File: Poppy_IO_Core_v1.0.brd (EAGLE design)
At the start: 67.6 x 31.8 mm, 97 parts, among them IC3 ATMEGA2560-16AU, IC6 LP2985-33DBVR, Q1 16MHz, Q2 16MHz, Q3 16MHz, Q4 16MHz, Q5 24MHz, U1 ATmega16u2, U2 MPU-6000, U3 USB2514B-AEZC, U4 ATmega16u2, U5 ATmega16u2, X1 1376408-SLOT_1.8V

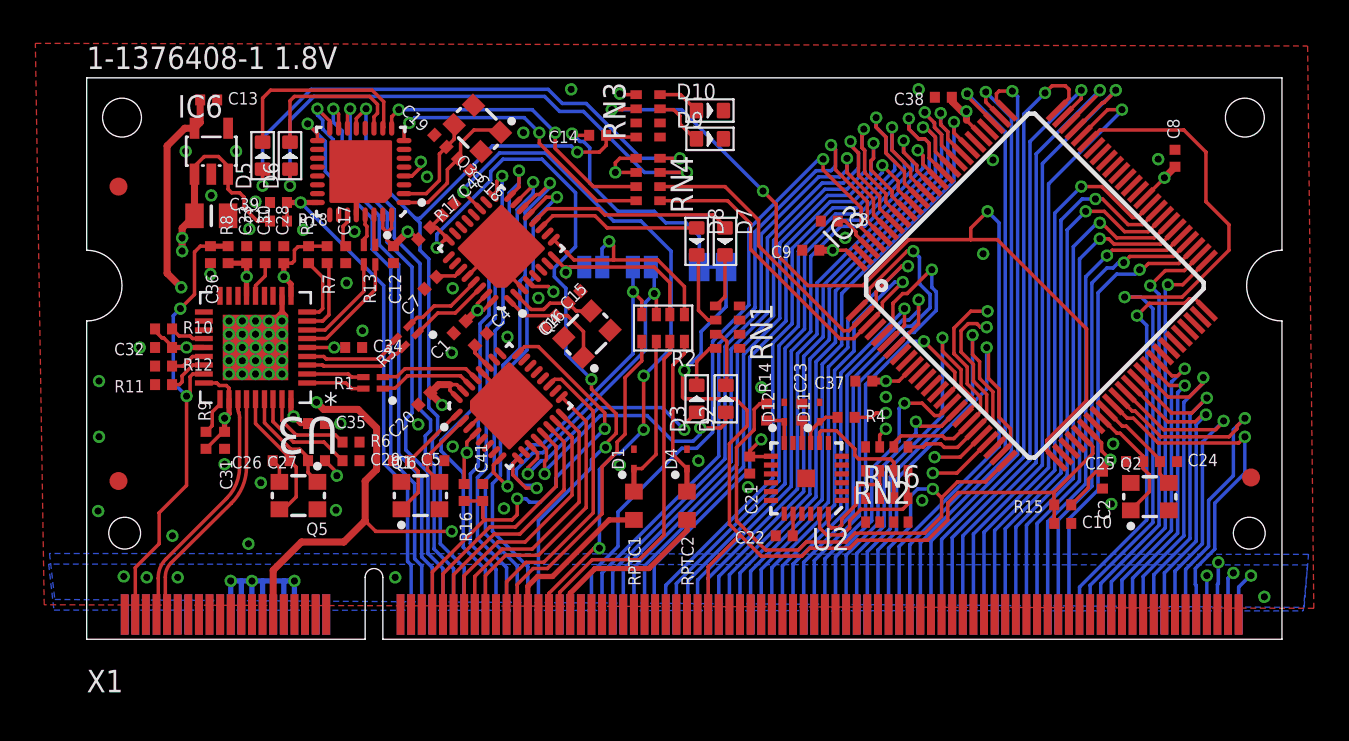
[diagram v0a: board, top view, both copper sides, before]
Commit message: Connected some (important) signals that had been omitted.
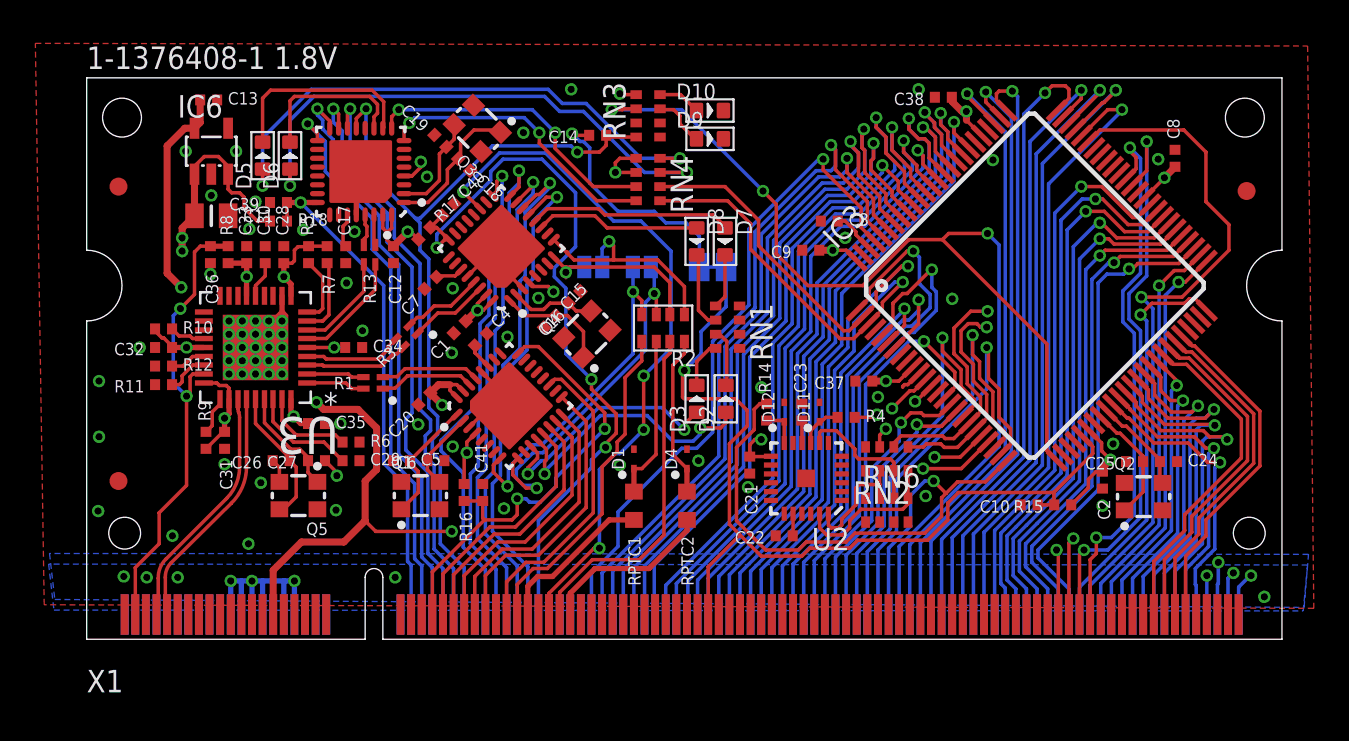
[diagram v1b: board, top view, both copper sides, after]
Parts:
- moved FD3 16.2 mm to (65.6, 25.4)
- moved C10 2.17 mm to (53.3, 7.60), turned to 180 degrees
- moved Q2 0.35 mm to (59.8, 8.04)
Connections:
- net GND: no longer X1.165, X1.167, X1.169, X1.171, X1.173, X1.175, X1.177, X1.179, X1.181, X1.183, X1.185, X1.187, X1.189, X1.191, X1.193, X1.195
- net RXD1: now also X1.187
- net RXD2: now also X1.165
- net RXD3: now also X1.169
- net SCL: now also X1.183
- net SDA: now also X1.185
- net TXD1: now also X1.189
- net TXD2: now also X1.167
- net TXD3: now also X1.171
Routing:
- net RXD3: track 0.00 -> 32.5 mm, vias 0 -> 2
- net TXD3: track 0.00 -> 31.0 mm, vias 0 -> 2
- net RXD2: track 0.00 -> 19.6 mm, vias 0 -> 2
- net TXD1: track 0.00 -> 19.4 mm
- net RXD1: track 0.00 -> 19.3 mm
- net SDA: track 0.00 -> 19.2 mm
- net SCL: track 0.00 -> 19.0 mm
- net TXD2: track 0.00 -> 18.6 mm, vias 0 -> 2
- net PL1: track 21.0 -> 16.6 mm
- net L13: track 73.2 -> 69.0 mm
- net PL0: track 19.7 -> 16.6 mm
- net PG2: track 41.2 -> 39.3 mm
- net PC0: track 25.4 -> 27.1 mm
- net PL5: track 19.3 -> 17.6 mm
- net PL7: track 17.5 -> 16.1 mm
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
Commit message: Aesthetics of the board done (text / logos)
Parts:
- added U$1, U$3: (no value), SparkFun-Aesthetics:OSHW-LOGO-M
- added U$2, U$4: (no value), cc-by-sa:CC-BY-SA
- moved FD3 24.3 mm to (50.7, 6.15)
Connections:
- net GND: now also X1.173, X1.181, X1.191; no longer X1.103, X1.105, X1.107, X1.109, X1.111, X1.113, X1.115, X1.117, X1.119, X1.121, X1.123, X1.125, X1.127, X1.129, X1.131, X1.133, X1.135, X1.137, X1.139, X1.141, X1.143, X1.145, X1.147, X1.149, X1.151, X1.153, X1.155, X1.157, X1.159, X1.161, X1.197
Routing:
- net +5V: track 67.8 -> 69.0 mm
- net L13: track 69.0 -> 70.0 mm
- net N$54: track 31.1 -> 31.7 mm
- net N$55: track 31.0 -> 31.5 mm
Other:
- board text added: "1"
- board text added: "199"
- board text added: "2"
- board text added: "200"
- board text added: "39"
- board text added: "40"
- board text added: "DXL1"
- board text added: "DXL2"
- board text added: "Design by Nicolas Saugnier"
- board text added: "LED"
- board text added: "Open source robotics for Research, Art and Education"
- board text added: "PWR"
- board text added: "Poppy IO module v1.0"
- board text added: "RST-EN"
- board text added: "RX"
- board text added: "SJ1"
- board text added: "SJ2"
- board text added: "TX"
- board text added: "www.poppy-project.org"

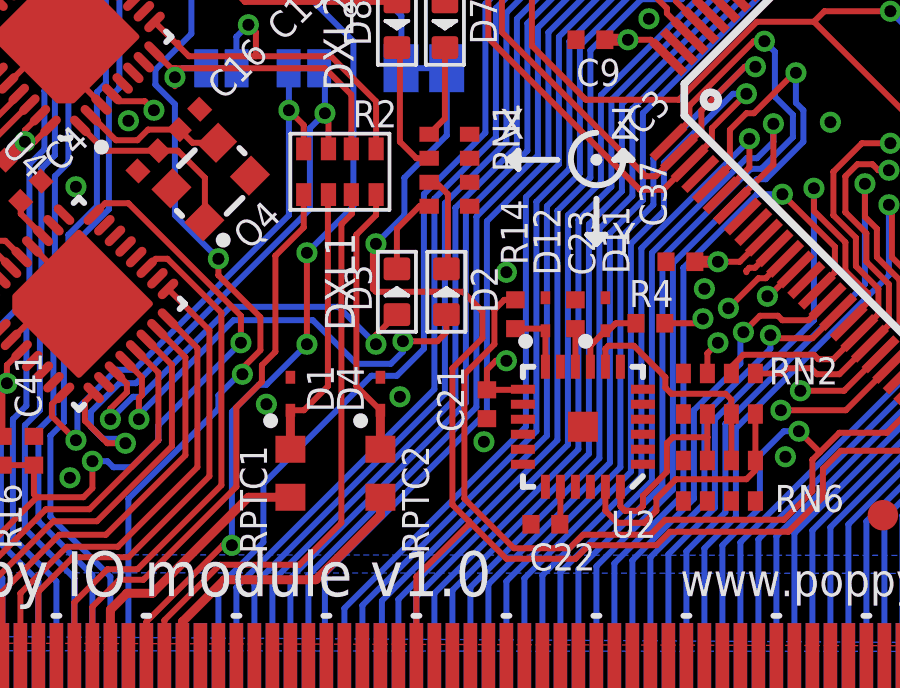
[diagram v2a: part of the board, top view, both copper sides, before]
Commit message: Replaced 3.3V SOD-923 LEDs with ones easier to source.
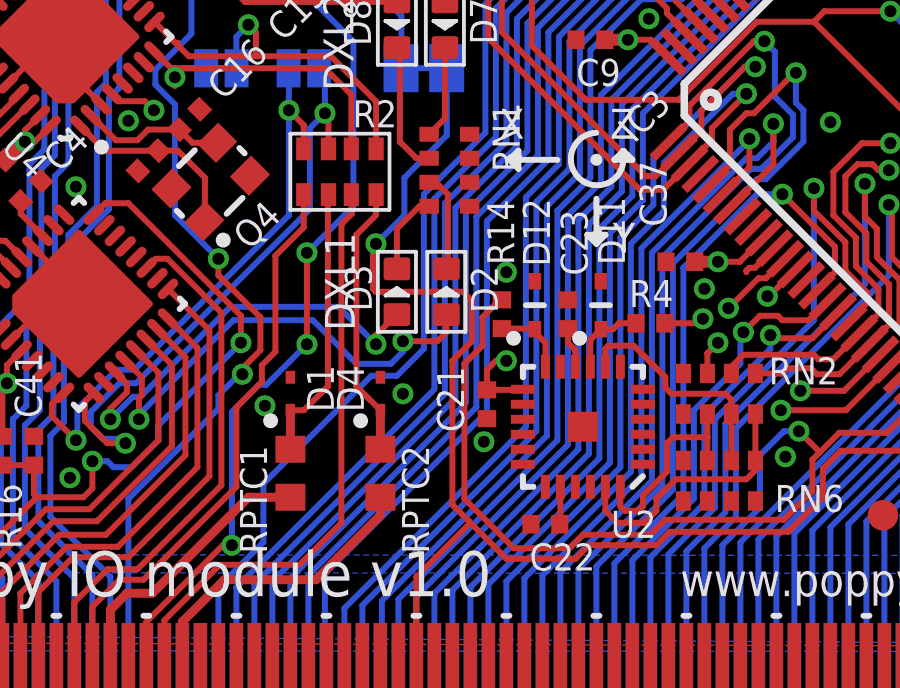
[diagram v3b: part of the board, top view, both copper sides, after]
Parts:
- D11, D12: device Xevelabs:SOD-923_N -> Xevelabs:SOD-523_N
- moved D12 0.46 mm to (39.1, 13.2)
- moved R14 0.45 mm to (38.0, 12.8)
- moved D11 0.34 mm to (41.3, 13.2)
- moved C23 0.25 mm to (40.2, 12.8)
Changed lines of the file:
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@@
 <setting verticaltext="up"/>
 </settings>
-<grid distance="0.06" unitdist="mm" unit="mm" style="dots" multiple="1" display="yes" altdistance="0.025" altunitdist="inch" altunit="inch"/>
+<grid distance="0.05" unitdist="mm" unit="mm" style="dots" multiple="1" display="yes" altdistance="0.025" altunitdist="inch" altunit="inch"/>
 <layers>
 <layer number="1" name="Top" color="4" fill="1" visible="yes" active="yes"/>
-<layer number="2" name="Route2" color="1" fill="3" visible="no" active="yes"/>
+<layer number="2" name="Route2" color="1" fill="3" visible="yes" active="yes"/>
 <layer number="3" name="Route3" color="4" fill="3" visible="no" active="no"/>
 <layer number="14" name="Route14" color="1" fill="6" visible="no" active="no"/>
-<layer number="15" name="Route15" color="4" fill="6" visible="no" active="yes"/>
-<layer number="16" name="Bottom" color="1" fill="1" visible="no" active="yes"/>
+<layer number="15" name="Route15" color="4" fill="6" visible="yes" active="yes"/>
+<layer number="16" name="Bottom" color="1" fill="1" visible="yes" active="yes"/>
 <layer number="17" name="Pads" color="2" fill="1" visible="yes" active="yes"/>
 <layer number="18" name="Vias" color="2" fill="1" visible="yes" active="yes"/>
@@
 <layer number="21" name="tPlace" color="7" fill="1" visible="yes" active="yes"/>
 <layer number="22" name="bPlace" color="7" fill="1" visible="no" active="yes"/>
-<layer number="23" name="tOrigins" color="15" fill="1" visible="no" active="yes"/>
+<layer number="23" name="tOrigins" color="15" fill="1" visible="yes" active="yes"/>
 <layer number="24" name="bOrigins" color="15" fill="1" visible="no" active="yes"/>
 <layer number="25" name="tNames" color="7" fill="1" visible="no" active="yes"/>
@@
 <layer number="37" name="tTest" color="7" fill="1" visible="no" active="yes"/>
 <layer number="38" name="bTest" color="7" fill="1" visible="no" active="yes"/>
-<layer number="39" name="tKeepout" color="4" fill="11" visible="no" active="yes"/>
+<layer number="39" name="tKeepout" color="4" fill="11" visible="yes" active="yes"/>
 <layer number="40" name="bKeepout" color="1" fill="11" visible="no" active="yes"/>
 <layer number="41" name="tRestrict" color="4" fill="10" visible="no" active="yes"/>
@@
 <attribute name="VALUE" x="40.42" y="5.18" size="0.7" layer="27" ratio="5" rot="R180"/>
 </element>
-<element name="C23" library="Xevelabs" package="0402_N" value="0.1uF" x="40.45" y="12.85" smashed="yes" rot="R90">
-<attribute name="NAME" x="41.11" y="14.14" size="0.9" layer="25" ratio="17" rot="R90"/>
-<attribute name="VALUE" x="39.78" y="11.88" size="0.7" layer="27" ratio="5" rot="R90"/>
+<element name="C23" library="Xevelabs" package="0402_N" value="0.1uF" x="40.2" y="12.85" smashed="yes" rot="R90">
+<attribute name="NAME" x="40.86" y="14.14" size="0.9" layer="25" ratio="17" rot="R90"/>
+<attribute name="VALUE" x="39.53" y="11.88" size="0.7" layer="27" ratio="5" rot="R90"/>
 </element>
 <element name="C18" library="Xevelabs" package="0402_N" value="18pF" x="21.35146875" y="26.837259375" smashed="yes" rot="R315">
@@
 <attribute name="VALUE" x="41.98" y="13.22" size="0.7" layer="27" ratio="5"/>
 </element>
-<element name="R14" library="Xevelabs" package="0402_N" value="470R" x="38.45" y="12.85" smashed="yes" rot="R90">
-<attribute name="NAME" x="38.86" y="14.49" size="0.9" layer="25" ratio="17" rot="R90"/>
-<attribute name="VALUE" x="37.78" y="11.88" size="0.7" layer="27" ratio="5" rot="R90"/>
+<element name="R14" library="Xevelabs" package="0402_N" value="470R" x="38" y="12.85" smashed="yes" rot="R90">
+<attribute name="NAME" x="38.41" y="14.49" size="0.9" layer="25" ratio="17" rot="R90"/>
+<attribute name="VALUE" x="37.33" y="11.88" size="0.7" layer="27" ratio="5" rot="R90"/>
 </element>
 <element name="RN2" library="resistor-dil" package="CAT16" value="10K" x="45.25" y="10.2" smashed="yes">
@@
 <attribute name="VALUE" x="47.155" y="6.03" size="1.27" layer="27" ratio="10" rot="R180"/>
 </element>
-<element name="D11" library="Xevelabs" package="SOD-923_N" value="3.3V" x="41.45" y="12.85" smashed="yes" rot="R90">
-<attribute name="NAME" x="42.25" y="14.19" size="0.9" layer="25" ratio="17" rot="R90"/>
-<attribute name="VALUE" x="41.66" y="13.79" size="0.7" layer="27" ratio="5" rot="R90"/>
-</element>
-<element name="D12" library="Xevelabs" package="SOD-923_N" value="3.3V" x="39.45" y="12.85" smashed="yes" rot="R90">
-<attribute name="NAME" x="39.95" y="14.14" size="0.9" layer="25" ratio="17" rot="R90"/>
-<attribute name="VALUE" x="39.66" y="13.79" size="0.7" layer="27" ratio="5" rot="R90"/>
+<element name="D11" library="Xevelabs" package="SOD-523_N" value="3.3V" x="41.3" y="13.15" smashed="yes" rot="R90">
+<attribute name="NAME" x="42.1" y="14.49" size="0.9" layer="25" ratio="17" rot="R90"/>
+<attribute name="VALUE" x="41.51" y="14.09" size="0.7" layer="27" ratio="5" rot="R90"/>
+</element>
+<element name="D12" library="Xevelabs" package="SOD-523_N" value="3.3V" x="39.1" y="13.15" smashed="yes" rot="R90">
+<attribute name="NAME" x="39.6" y="14.44" size="0.9" layer="25" ratio="17" rot="R90"/>
+<attribute name="VALUE" x="39.31" y="14.09" size="0.7" layer="27" ratio="5" rot="R90"/>
 </element>
 <element name="R15" library="Xevelabs" package="0402_N" value="10k" x="55.2" y="7.6" smashed="yes" rot="R180">
@@
 <via x="23.6" y="7.4" extent="1-16" drill="0.4"/>
 <contactref element="RN3" pad="5"/>
-<via x="30.15" y="9.85" extent="1-16" drill="0.4"/>
-<via x="34.6" y="10.1" extent="1-16" drill="0.4"/>
+<via x="30.1" y="9.8" extent="1-16" drill="0.4"/>
+<via x="34.7" y="10.2" extent="1-16" drill="0.4"/>
 <contactref element="RN1" pad="2"/>
 <contactref element="RN1" pad="1"/>
@@
 <wire x1="38.15" y1="4.7" x2="36.9" y2="5.95" width="0.2" layer="1"/>
 <wire x1="36.9" y1="5.95" x2="36.35" y2="6.5" width="0.2" layer="1"/>
-<wire x1="36.35" y1="6.5" x2="36.35" y2="11.05" width="0.2" layer="1"/>
-<wire x1="36.35" y1="11.05" x2="37.35" y2="12.05" width="0.2" layer="1"/>
+<wire x1="36.35" y1="6.5" x2="36.35" y2="11.3" width="0.2" layer="1"/>
+<wire x1="36.35" y1="11.3" x2="37" y2="11.95" width="0.2" layer="1"/>
 <via x="33.8" y="15.2" extent="1-16" drill="0.4"/>
 <wire x1="34.638" y1="21.05" x2="36.162" y2="21.05" width="0.2" layer="16"/>
@@
 <wire x1="35.15" y1="4.1" x2="36.9" y2="5.85" width="0.2" layer="1"/>
 <wire x1="36.9" y1="5.85" x2="36.9" y2="5.95" width="0.2" layer="1"/>
-<wire x1="37.35" y1="12.05" x2="37.35" y2="12.95" width="0.2" layer="1"/>
-<wire x1="37.35" y1="12.95" x2="36.7" y2="13.6" width="0.2" layer="1"/>
+<wire x1="37" y1="11.95" x2="37" y2="13.3" width="0.2" layer="1"/>
+<wire x1="37" y1="13.3" x2="36.7" y2="13.6" width="0.2" layer="1"/>
 <wire x1="36.7" y1="13.6" x2="33.8" y2="13.6" width="0.2" layer="1"/>
 <wire x1="33.8" y1="13.6" x2="33.7" y2="13.7" width="0.2" layer="1"/>
@@
 <contactref element="IC3" pad="25"/>
 <contactref element="R14" pad="2"/>
-<wire x1="38.45" y1="13.33" x2="38.08" y2="13.33" width="0.2" layer="1"/>
-<wire x1="38.08" y1="13.33" x2="37.75" y2="13" width="0.2" layer="1"/>
-<wire x1="37.75" y1="13" x2="37.75" y2="11.85" width="0.2" layer="1"/>
-<wire x1="37.75" y1="11.85" x2="36.75" y2="10.85" width="0.2" layer="1"/>
-<wire x1="36.75" y1="10.85" x2="36.75" y2="6.7" width="0.2" layer="1"/>
+<wire x1="38" y1="13.33" x2="37.93" y2="13.33" width="0.2" layer="1"/>
+<wire x1="37.93" y1="13.33" x2="37.35" y2="12.75" width="0.2" layer="1"/>
+<wire x1="37.35" y1="12.75" x2="37.35" y2="11.8" width="0.2" layer="1"/>
+<wire x1="37.35" y1="11.8" x2="36.75" y2="11.2" width="0.2" layer="1"/>
+<wire x1="36.75" y1="11.2" x2="36.75" y2="6.7" width="0.2" layer="1"/>
 <wire x1="36.75" y1="6.7" x2="38.4" y2="5.05" width="0.2" layer="1"/>
 <wire x1="38.4" y1="5.05" x2="40.25" y2="5.05" width="0.2" layer="1"/>
@@
 <contactref element="R4" pad="1"/>
 <contactref element="D11" pad="C"/>
-<wire x1="40.95" y1="11.1" x2="40.95" y2="11.8" width="0.2" layer="1"/>
-<wire x1="40.95" y1="11.8" x2="41.45" y2="12.3" width="0.2" layer="1"/>
-<wire x1="41.45" y1="12.3" x2="41.5" y2="12.25" width="0.2" layer="1"/>
-<wire x1="41.5" y1="12.25" x2="41.8" y2="12.55" width="0.2" layer="1"/>
-<wire x1="41.8" y1="12.55" x2="42.47" y2="12.55" width="0.2" layer="1"/>
+<wire x1="40.95" y1="11.1" x2="40.95" y2="12" width="0.2" layer="1"/>
+<wire x1="40.95" y1="12" x2="41.3" y2="12.35" width="0.2" layer="1"/>
+<wire x1="41.3" y1="12.35" x2="41.7" y2="12.35" width="0.2" layer="1"/>
+<wire x1="41.7" y1="12.35" x2="41.9" y2="12.55" width="0.2" layer="1"/>
+<wire x1="41.9" y1="12.55" x2="42.47" y2="12.55" width="0.2" layer="1"/>
 </signal>
 <signal name="!CS_3V3">
@@
 <contactref element="U2" pad="10"/>
 <contactref element="C23" pad="1"/>
-<wire x1="40.45" y1="12.37" x2="40.45" y2="11.1" width="0.2" layer="1"/>
+<wire x1="40.2" y1="12.37" x2="40.2" y2="11.9" width="0.2" layer="1"/>
+<wire x1="40.2" y1="11.9" x2="40.45" y2="11.65" width="0.2" layer="1"/>
+<wire x1="40.45" y1="11.65" x2="40.45" y2="11.1" width="0.2" layer="1"/>
 </signal>
 <signal name="MPU_INT">
@@
 <contactref element="R14" pad="1"/>
 <contactref element="D12" pad="C"/>
-<wire x1="39.45" y1="11.1" x2="39.45" y2="12.3" width="0.2" layer="1"/>
-<wire x1="39.45" y1="12.3" x2="39.38" y2="12.37" width="0.2" layer="1"/>
-<wire x1="39.38" y1="12.37" x2="38.45" y2="12.37" width="0.2" layer="1"/>
+<wire x1="39.45" y1="11.1" x2="39.45" y2="11.9" width="0.2" layer="1"/>
+<wire x1="39.45" y1="11.9" x2="39.1" y2="12.25" width="0.2" layer="1"/>
+<wire x1="39.1" y1="12.25" x2="39.1" y2="12.35" width="0.2" layer="1"/>
+<wire x1="39.1" y1="12.35" x2="38.93" y2="12.37" width="0.2" layer="1"/>
+<wire x1="38.93" y1="12.37" x2="38" y2="12.37" width="0.2" layer="1"/>
 </signal>
 <signal name="USBDM_UP">
